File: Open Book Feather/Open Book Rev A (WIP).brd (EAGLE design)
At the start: 77.5 x 112.3 mm, 111 parts, among them J1 SJ-43514-SMT, J2 10118193-0001LF, Q1 DMG341, Q2 IRLML0100, SW1 SPDT_SWITCH, U1 AP2112-3.3, U2 MCP73831T-2ACI/OT, U3 ATSAMD51J64-TQFP(10X10), U4 GD25Q64, U5 74AC165D, U7 23K256-I/SN, X1 JSTPH, X2 2x5 0.05" SWD

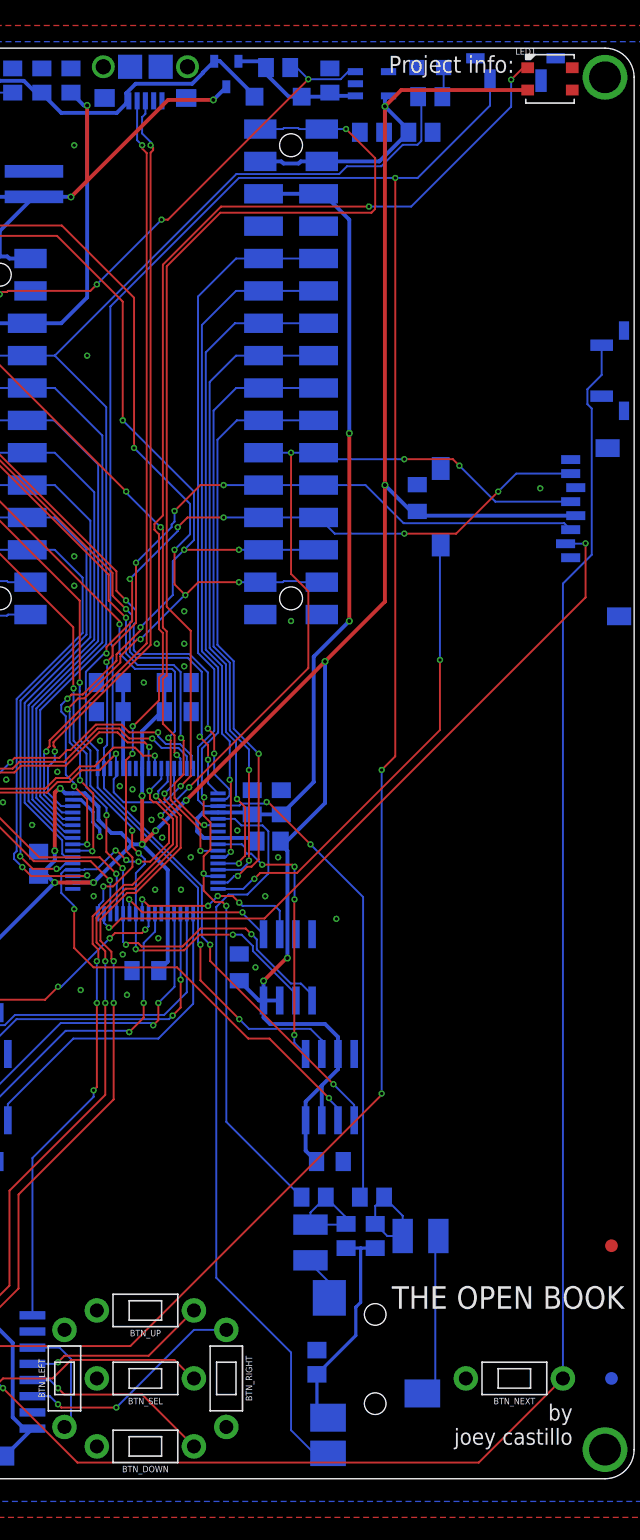
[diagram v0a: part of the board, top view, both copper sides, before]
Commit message: move traces out of text areas
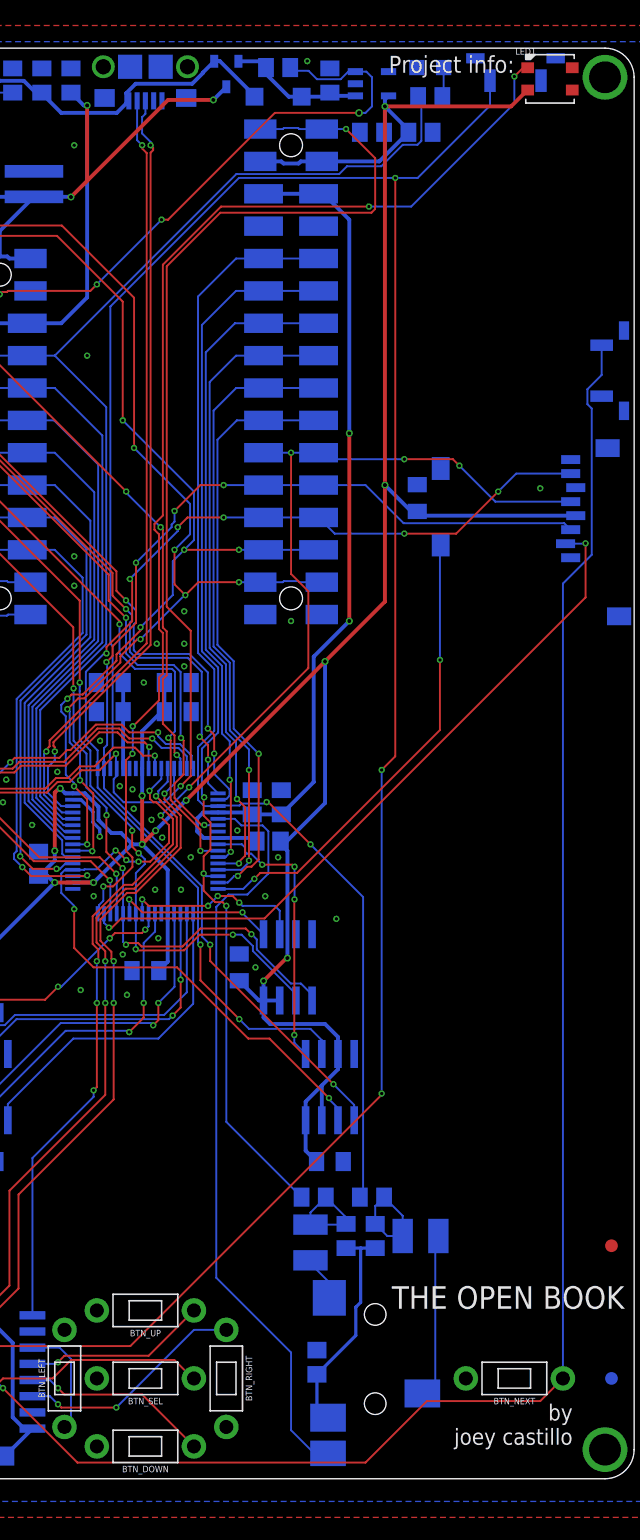
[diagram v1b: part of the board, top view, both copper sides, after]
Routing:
- net EN: track 144.2 -> 152.5 mm
- net GND: vias 36 -> 37
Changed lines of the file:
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@@
 <wire x1="33.162" y1="53.288" x2="33.80713125" y2="53.288" width="0.254" layer="16"/>
 <wire x1="33.80713125" y1="53.288" x2="34.7472" y2="52.34793125" width="0.254" layer="16"/>
+<via x="51.562" y="111.252" extent="1-16" drill="0.254"/>
 </signal>
 <signal name="EINK_CS">
@@
 <wire x1="55.3419" y1="110.424" x2="54.7792875" y2="110.424" width="0.1524" layer="16"/>
 <wire x1="54.7792875" y1="110.424" x2="54.1846875" y2="109.8294" width="0.1524" layer="16"/>
-<wire x1="54.1846875" y1="109.8294" x2="51.6486" y2="109.8294" width="0.1524" layer="16"/>
-<wire x1="51.6486" y1="109.8294" x2="50.734" y2="110.744" width="0.1524" layer="16"/>
+<wire x1="54.1846875" y1="109.8294" x2="52.324" y2="109.8294" width="0.1524" layer="16"/>
 <wire x1="50.734" y1="110.744" x2="50.226" y2="110.744" width="0.1524" layer="16"/>
-<via x="51.6486" y="109.8294" extent="1-16" drill="0.254"/>
-<wire x1="51.6486" y1="109.8294" x2="40.6252" y2="98.806" width="0.1524" layer="1"/>
-<wire x1="40.132" y1="98.806" x2="40.6252" y2="98.806" width="0.1524" layer="1"/>
 <via x="40.132" y="98.806" extent="1-16" drill="0.254"/>
 <wire x1="40.132" y1="98.806" x2="35.052" y2="93.726" width="0.1524" layer="16"/>
@@
 <wire x1="15.255409375" y1="82.311409375" x2="15.255409375" y2="86.364409375" width="0.1524" layer="1"/>
 <wire x1="15.255409375" y1="86.364409375" x2="21.082" y2="92.191" width="0.1524" layer="1"/>
+<wire x1="50.48" y1="110.49" x2="50.226" y2="110.744" width="0.1524" layer="16"/>
+<wire x1="52.324" y1="109.8294" x2="51.6634" y2="110.49" width="0.1524" layer="16"/>
+<wire x1="51.6634" y1="110.49" x2="50.48" y2="110.49" width="0.1524" layer="16"/>
+<wire x1="55.3419" y1="110.424" x2="56.2" y2="110.424" width="0.1524" layer="16"/>
+<wire x1="56.2" y1="110.424" x2="56.642" y2="109.982" width="0.1524" layer="16"/>
+<wire x1="56.642" y1="109.982" x2="56.642" y2="107.696" width="0.1524" layer="16"/>
+<via x="55.626" y="107.188" extent="1-16" drill="0.35"/>
+<wire x1="55.626" y1="107.188" x2="49.022" y2="107.188" width="0.1524" layer="1"/>
+<wire x1="56.642" y1="107.696" x2="56.134" y2="107.188" width="0.1524" layer="16"/>
+<wire x1="56.134" y1="107.188" x2="55.626" y2="107.188" width="0.1524" layer="16"/>
+<wire x1="49.022" y1="107.188" x2="40.64" y2="98.806" width="0.1524" layer="1"/>
+<wire x1="40.64" y1="98.806" x2="40.132" y2="98.806" width="0.1524" layer="1"/>
 </signal>
 <signal name="+3V3" class="1">
@@
 <wire x1="57.658" y1="108.2399" x2="57.658" y2="107.696" width="0.3048" layer="16"/>
 <via x="57.658" y="107.696" extent="1-16" drill="0.3048"/>
-<wire x1="57.658" y1="107.696" x2="58.942" y2="108.98" width="0.3048" layer="1"/>
-<wire x1="58.942" y1="108.98" x2="68.862" y2="108.98" width="0.3048" layer="1"/>
+<wire x1="68.848" y1="108.98" x2="67.564" y2="107.696" width="0.3048" layer="1"/>
+<wire x1="57.658" y1="107.696" x2="67.564" y2="107.696" width="0.3048" layer="1"/>
+<wire x1="68.848" y1="108.98" x2="68.862" y2="108.98" width="0.3048" layer="1"/>
 <contactref element="MS2" pad="2'"/>
 <contactref element="MS2" pad="2"/>
@@
 <contactref element="LED1" pad="1"/>
 <wire x1="68.862" y1="110.73" x2="68.5012" y2="110.73" width="0.1524" layer="1"/>
-<wire x1="68.5012" y1="110.73" x2="67.564" y2="109.7928" width="0.1524" layer="1"/>
-<via x="67.564" y="109.7928" extent="1-16" drill="0.254"/>
-<wire x1="67.564" y1="109.7928" x2="67.564" y2="107.6801125" width="0.1524" layer="16"/>
-<wire x1="67.564" y1="107.6801125" x2="59.720021875" y2="99.836134375" width="0.1524" layer="16"/>
+<wire x1="68.5012" y1="110.73" x2="67.818" y2="110.0468" width="0.1524" layer="1"/>
+<via x="67.818" y="110.0468" extent="1-16" drill="0.254"/>
+<wire x1="67.818" y1="110.0468" x2="67.818" y2="107.9341125" width="0.1524" layer="16"/>
+<wire x1="67.818" y1="107.9341125" x2="59.720021875" y2="99.836134375" width="0.1524" layer="16"/>
 <wire x1="56.402134375" y1="99.836134375" x2="59.720021875" y2="99.836134375" width="0.1524" layer="16"/>
 <via x="56.402134375" y="99.836134375" extent="1-16" drill="0.254"/>
@@
 <contactref element="BTN_NEXT" pad="P$1"/>
 <contactref element="BTN_NEXT_ALT" pad="P$1"/>
-<wire x1="71.628" y1="7.874" x2="65.024" y2="1.27" width="0.1524" layer="1"/>
+<wire x1="69.85" y1="6.096" x2="71.628" y2="7.874" width="0.1524" layer="1"/>
 <wire x1="27.686" y1="7.112" x2="25.781" y2="9.017" width="0.1524" layer="16"/>
 <wire x1="25.781" y1="9.017" x2="23.8506" y2="9.017" width="0.1524" layer="16"/>
 <via x="27.686" y="7.112" extent="1-16" drill="0.254"/>
 <wire x1="33.528" y1="1.27" x2="27.686" y2="7.112" width="0.1524" layer="1"/>
-<wire x1="65.024" y1="1.27" x2="33.528" y2="1.27" width="0.1524" layer="1"/>
+<wire x1="56.134" y1="1.27" x2="33.528" y2="1.27" width="0.1524" layer="1"/>
 <wire x1="74.6664" y1="88.9558" x2="74.6664" y2="86.6180875" width="0.1524" layer="16"/>
 <wire x1="74.6664" y1="86.6180875" x2="73.5488" y2="85.5004875" width="0.1524" layer="16"/>
@@
 <wire x1="73.8886" y1="83.9882" x2="73.5488" y2="84.328" width="0.1524" layer="16"/>
 <wire x1="73.8886" y1="72.5103125" x2="73.8886" y2="83.9882" width="0.1524" layer="16"/>
+<wire x1="56.134" y1="1.27" x2="60.96" y2="6.096" width="0.1524" layer="1"/>
+<wire x1="60.96" y1="6.096" x2="69.85" y2="6.096" width="0.1524" layer="1"/>
 </signal>
 <signal name="BUTTON7">

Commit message: also tent power vias
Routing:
- net EN: track 152.5 -> 152.0 mm
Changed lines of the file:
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@@
 <param name="mlMinCreamFrame" value="0mil"/>
 <param name="mlMaxCreamFrame" value="0mil"/>
-<param name="mlViaStopLimit" value="10mil"/>
+<param name="mlViaStopLimit" value="12mil"/>
 <param name="srRoundness" value="0"/>
 <param name="srMinRoundness" value="0mil"/>
@@
 <wire x1="54.7792875" y1="110.424" x2="54.1846875" y2="109.8294" width="0.1524" layer="16"/>
 <wire x1="54.1846875" y1="109.8294" x2="52.324" y2="109.8294" width="0.1524" layer="16"/>
-<wire x1="50.734" y1="110.744" x2="50.226" y2="110.744" width="0.1524" layer="16"/>
 <via x="40.132" y="98.806" extent="1-16" drill="0.254"/>
 <wire x1="40.132" y1="98.806" x2="35.052" y2="93.726" width="0.1524" layer="16"/>
